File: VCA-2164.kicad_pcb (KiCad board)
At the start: 2 copper layers, 80 x 95 mm, 87 parts, among them J14 Conn_02x05_Odd_Even, J15 Conn_01x01, J16 Conn_01x01, J17 Conn_01x01, J18 Conn_01x01, J19 Conn_01x01, J20 Conn_01x01, J21 Conn_01x01, J22 Conn_01x01, J23 Conn_01x01, J24 Conn_01x01, J25 Conn_01x01, J26 Conn_01x01, J27 Conn_01x01, J28 Conn_01x01, J29 Conn_01x01, J30 Conn_01x01, J31 Conn_01x01, U1 TL074, U2 AS2164, U3 TL074, U4 TL072

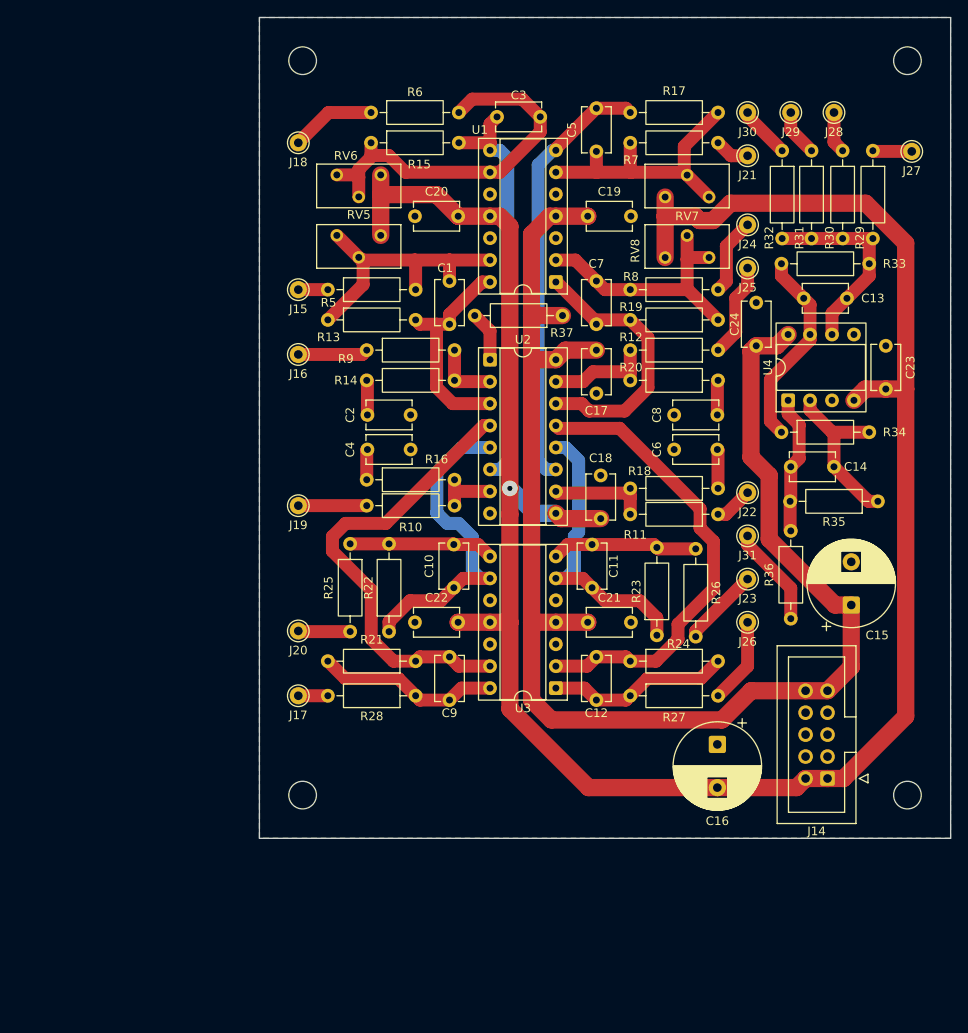
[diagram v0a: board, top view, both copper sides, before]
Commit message: non inverting outputs, peak indicator LED
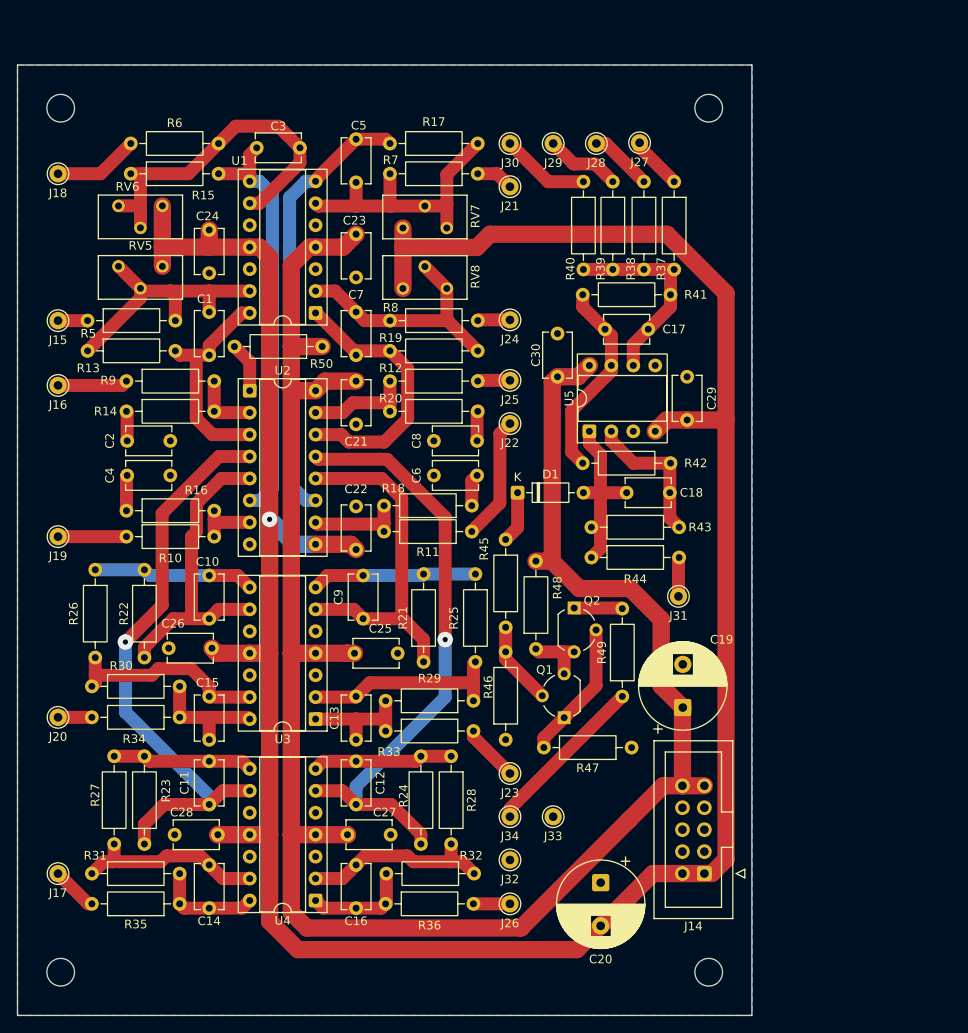
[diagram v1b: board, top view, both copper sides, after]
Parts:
- added C10: 100p, Capacitor_THT:C_Disc_D5.1mm_W3.2mm_P5.00mm, F.Cu at (129.2, 108.6)
- added C11: 100p, Capacitor_THT:C_Disc_D5.1mm_W3.2mm_P5.00mm, F.Cu at (129.2, 130.1)
- added C12: 100p, Capacitor_THT:C_Disc_D5.1mm_W3.2mm_P5.00mm, F.Cu at (146.2, 130.1)
- added C27: 0.1u, Capacitor_THT:C_Disc_D5.1mm_W3.2mm_P5.00mm, F.Cu at (145.2, 133.6)
- added C28: 0.1u, Capacitor_THT:C_Disc_D5.1mm_W3.2mm_P5.00mm, F.Cu at (125.2, 133.6)
- added C9: 100p, Capacitor_THT:C_Disc_D5.1mm_W3.2mm_P5.00mm, F.Cu at (147.0, 108.6)
- added D1: 1N4148, Diode_THT:D_DO-35_SOD27_P7.62mm_Horizontal, F.Cu at (164.9, 94.0)
- added J32: Conn_01x01, Connector_Pin:Pin_D1.0mm_L10.0mm, F.Cu at (164.0, 136.5)
- added J33: Conn_01x01, Connector_Pin:Pin_D1.0mm_L10.0mm, F.Cu at (169.0, 131.5)
- added J34: Conn_01x01, Connector_Pin:Pin_D1.0mm_L10.0mm, F.Cu at (164.0, 131.5)
- added Q1: BC556, Package_TO_SOT_THT:TO-92_Wide, F.Cu at (170.3, 120.0)
- added Q2: BC556, Package_TO_SOT_THT:TO-92_Wide, F.Cu at (171.4, 107.3)
- added R25: 10k, Resistor_THT:R_Axial_DIN0207_L6.3mm_D2.5mm_P10.16mm_Horizontal, F.Cu at (160.0, 103.4)
- added R26: 10k, Resistor_THT:R_Axial_DIN0207_L6.3mm_D2.5mm_P10.16mm_Horizontal, F.Cu at (116.0, 102.9)
- added R27: 10k, Resistor_THT:R_Axial_DIN0207_L6.3mm_D2.5mm_P10.16mm_Horizontal, F.Cu at (118.2, 124.5)
- added R28: 10k, Resistor_THT:R_Axial_DIN0207_L6.3mm_D2.5mm_P10.16mm_Horizontal, F.Cu at (157.2, 124.5)
- added R29: 10k, Resistor_THT:R_Axial_DIN0207_L6.3mm_D2.5mm_P10.16mm_Horizontal, F.Cu at (159.8, 118.1)
- added R30: 10k, Resistor_THT:R_Axial_DIN0207_L6.3mm_D2.5mm_P10.16mm_Horizontal, F.Cu at (115.6, 116.4)
- added R31: 10k, Resistor_THT:R_Axial_DIN0207_L6.3mm_D2.5mm_P10.16mm_Horizontal, F.Cu at (115.6, 138.1)
- added R32: 10k, Resistor_THT:R_Axial_DIN0207_L6.3mm_D2.5mm_P10.16mm_Horizontal, F.Cu at (159.8, 138.1)
- added R45: 10k, Resistor_THT:R_Axial_DIN0207_L6.3mm_D2.5mm_P10.16mm_Horizontal, F.Cu at (163.5, 99.4)
- added R46: 100k, Resistor_THT:R_Axial_DIN0207_L6.3mm_D2.5mm_P10.16mm_Horizontal, F.Cu at (163.5, 122.6)
- added R47: 750, Resistor_THT:R_Axial_DIN0207_L6.3mm_D2.5mm_P10.16mm_Horizontal, F.Cu at (178.1, 123.5)
- added R48: 750, Resistor_THT:R_Axial_DIN0207_L6.3mm_D2.5mm_P10.16mm_Horizontal, F.Cu at (167.0, 112.1)
- added R49: 750, Resistor_THT:R_Axial_DIN0207_L6.3mm_D2.5mm_P10.16mm_Horizontal, F.Cu at (177.0, 117.6)
- added U4: TL074, Package_DIP:DIP-14_W7.62mm_Socket, F.Cu at (141.5, 141.2)
- C13: renamed from C11; value 100p -> 22p
- C14: renamed from C9; value 100p -> 22p
- C15: renamed from C10; value 100p -> 22p
- C16: renamed from C12; value 100p -> 22p
- C17: renamed from C13; value 100p -> 22p
- C18: renamed from C14; value 100p -> 22p
- moved J26 42.6 mm to (164.0, 141.6)
- moved R33 41.6 mm to (149.6, 121.6), turned to 0 degrees
- moved R23 37.9 mm to (121.7, 134.7), turned to 90 degrees
- moved R36 37.2 mm to (149.6, 141.6)
- moved C14 36.8 mm to (129.2, 137.1)
- moved C16 36.8 mm to (146.2, 137.1)
- moved R35 36.4 mm to (125.8, 141.6)
- moved J23 35.5 mm to (164.0, 126.5)
- moved H1 34.7 mm to (112.0, 149.5)
- moved J17 34.6 mm to (111.7, 138.1)
- moved R24 32.2 mm to (153.7, 134.7), turned to 90 degrees
- moved J27 31.5 mm to (179.0, 53.5)
- moved C15 31.0 mm to (129.2, 117.6), turned to -90 degrees
- moved H4 30.8 mm to (187.0, 149.5)
- moved RV7 30.6 mm to (151.6, 63.4)
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- renumbered C15 to C19, C16 to C20, C17 to C21, C18 to C22, C19 to C23, C20 to C24, C21 to C25, C22 to C26, C23 to C29, C24 to C30, R23 to R21, R21 to R23, R26 to R33, R25 to R34, R28 to R35, R27 to R36, R29 to R37, R30 to R38, R31 to R39, R32 to R40, R33 to R41, R34 to R42, R35 to R43, R36 to R44, R37 to R50, U4 to U5
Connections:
- C13 pad 1: Net-(U3B--) -> Net-(U3A--)
- C13 pad 2: Net-(C11-Pad2) -> Net-(C13-Pad2)
- C14 pad 1: Net-(U3D--) -> Net-(U4D--)
- C14 pad 2: Net-(C9-Pad2) -> Net-(C14-Pad2)
- C15 pad 1: Net-(U3C--) -> Net-(U3D--)
- C15 pad 2: Net-(C10-Pad2) -> Net-(C15-Pad2)
- C16 pad 1: Net-(U3A--) -> Net-(U4A--)
- C16 pad 2: Net-(C12-Pad2) -> Net-(C16-Pad2)
- R21 pad 2: Net-(C11-Pad2) -> Net-(C9-Pad2)
- R23 pad 1: Net-(U3D--) -> Net-(U4C--)
- R23 pad 2: Net-(C9-Pad2) -> Net-(C11-Pad2)
- R24 pad 1: Net-(U3A--) -> Net-(U4B--)
- R33 pad 1: Net-(C11-Pad2) -> Net-(C13-Pad2)
- R34 pad 1: Net-(C10-Pad2) -> Net-(C15-Pad2)
- R35 pad 1: Net-(C9-Pad2) -> Net-(C14-Pad2)
- R36 pad 1: Net-(C12-Pad2) -> Net-(C16-Pad2)
- U2 pad 13: Net-(U3A--) -> Net-(U4B--)
- U2 pad 4: Net-(U3D--) -> Net-(U4C--)
- U3 pad 1: Net-(C12-Pad2) -> Net-(C13-Pad2)
- U3 pad 14: Net-(C9-Pad2) -> Net-(C15-Pad2)
- U3 pad 7: Net-(C11-Pad2) -> Net-(C9-Pad2)
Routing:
- net Net-(U4B--): track 0.00 -> 70.8 mm, vias 0 -> 1
- net Net-(U4C--): track 0.00 -> 68.4 mm, vias 0 -> 1
- net VCC: track 167.4 -> 228.1 mm
- net VEE: track 249.4 -> 303.8 mm
- net Net-(U3A--): track 54.0 -> 23.6 mm
- net Net-(U3D--): track 52.7 -> 23.8 mm
- net Net-(U4A--): track 0.00 -> 22.4 mm
- net Net-(U4D--): track 0.00 -> 22.3 mm
- net /LED_A: track 0.00 -> 19.3 mm
- net Net-(Q1-C): track 0.00 -> 16.1 mm
- net Net-(C15-Pad2): track 0.00 -> 14.4 mm
- net Net-(C13-Pad2): track 0.00 -> 14.0 mm
- net Net-(C16-Pad2): track 0.00 -> 12.2 mm
- net Net-(C14-Pad2): track 0.00 -> 12.2 mm
- net /IN_3: track 4.46 -> 14.3 mm
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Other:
- board size 80 x 95 mm -> 85 x 110 mm

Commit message: prettier solder pins arrangement
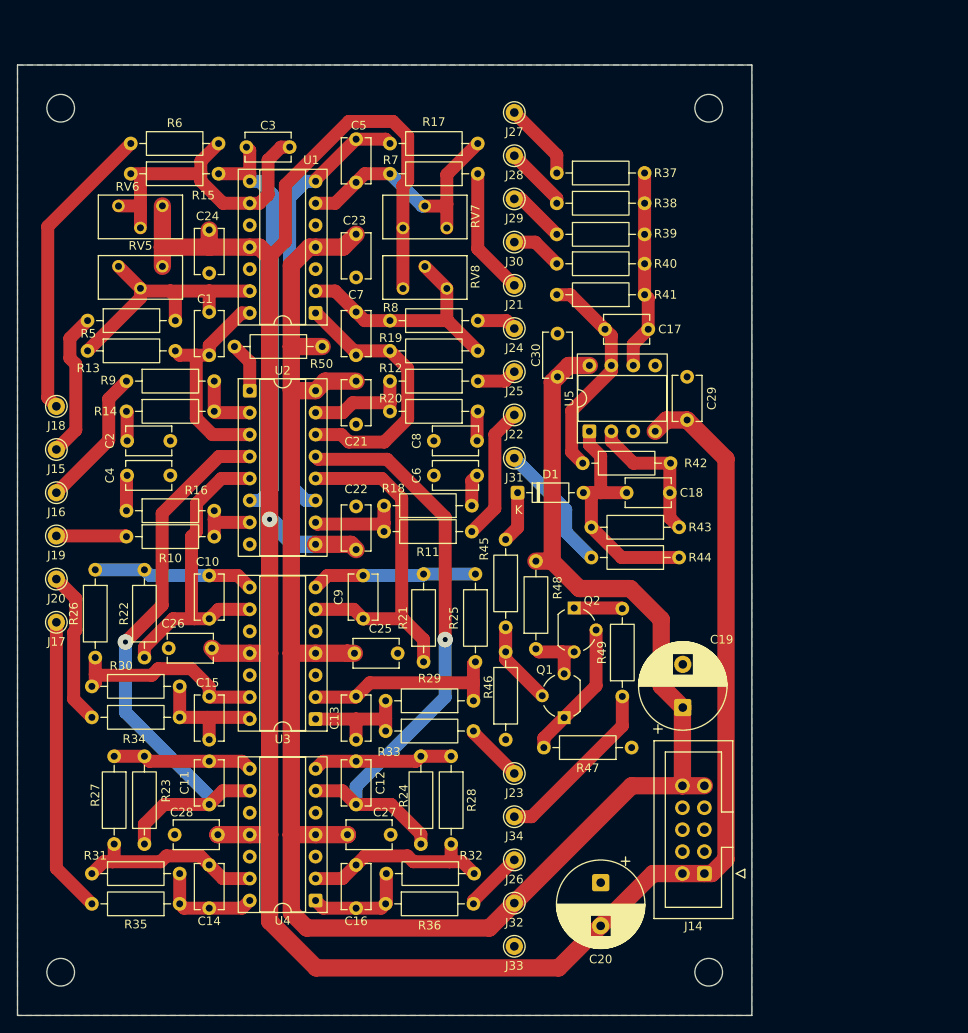
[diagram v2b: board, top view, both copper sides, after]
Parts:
- moved J17 29.1 mm to (111.5, 109.0)
- moved J18 26.9 mm to (111.5, 84.0)
- moved J31 24.8 mm to (164.5, 90.0)
- moved J20 16.0 mm to (111.5, 104.0)
- moved J33 15.7 mm to (164.5, 146.5)
- moved J27 14.9 mm to (164.5, 50.0)
- moved J15 14.9 mm to (111.5, 89.0)
- moved R37 13.6 mm to (169.4, 57.0), turned to 0 degrees
- moved J16 12.4 mm to (111.5, 94.0)
- moved J21 11.4 mm to (164.5, 70.0)
- moved J30 11.4 mm to (164.5, 65.0)
- moved R38 10.4 mm to (169.4, 60.5), turned to 0 degrees
- moved R44 10.2 mm to (183.6, 101.5), turned to 180 degrees
- moved R40 9.98 mm to (169.4, 67.5), turned to 0 degrees
- moved J28 9.60 mm to (164.5, 55.0)
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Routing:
- net /OUT_1: track 5.37 -> 34.3 mm
- net /CV_2: track 9.87 -> 34.8 mm
- net VEE: track 303.8 -> 285.2 mm
- net /OUT_2: track 3.92 -> 17.9 mm
- net /CV_1: track 3.42 -> 17.0 mm
- net /MIX_OUT: track 4.53 -> 15.2 mm
- net /CV_3: track 4.35 -> 14.7 mm
- net /IN_1: track 8.13 -> 16.3 mm
- net Net-(D1-A): track 20.6 -> 28.3 mm
- net /MIX_4: track 10.3 -> 5.96 mm
- net Net-(U1B--): track 33.2 -> 29.5 mm
- net /MIX_1: track 6.16 -> 9.04 mm
- net /OUT_4: track 4.23 -> 7.04 mm
- net Net-(U1C--): track 41.5 -> 38.8 mm
- net Net-(C17-Pad2): track 23.3 -> 25.5 mm
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
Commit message: unnecessary cap
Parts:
- removed the C17 at (180.0, 75.1)
- renumbered C18 to C17, C19 to C18, C20 to C19, C21 to C20, C22 to C21, C23 to C22, C24 to C23, C25 to C24, C26 to C25, C27 to C26, C28 to C27, C29 to C28, C30 to C29
